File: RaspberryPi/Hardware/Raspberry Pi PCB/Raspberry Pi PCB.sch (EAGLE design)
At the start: 30 parts, among them Q11 BSS138, Q12 BSS138, Q2 BSS138, X1 0446200002

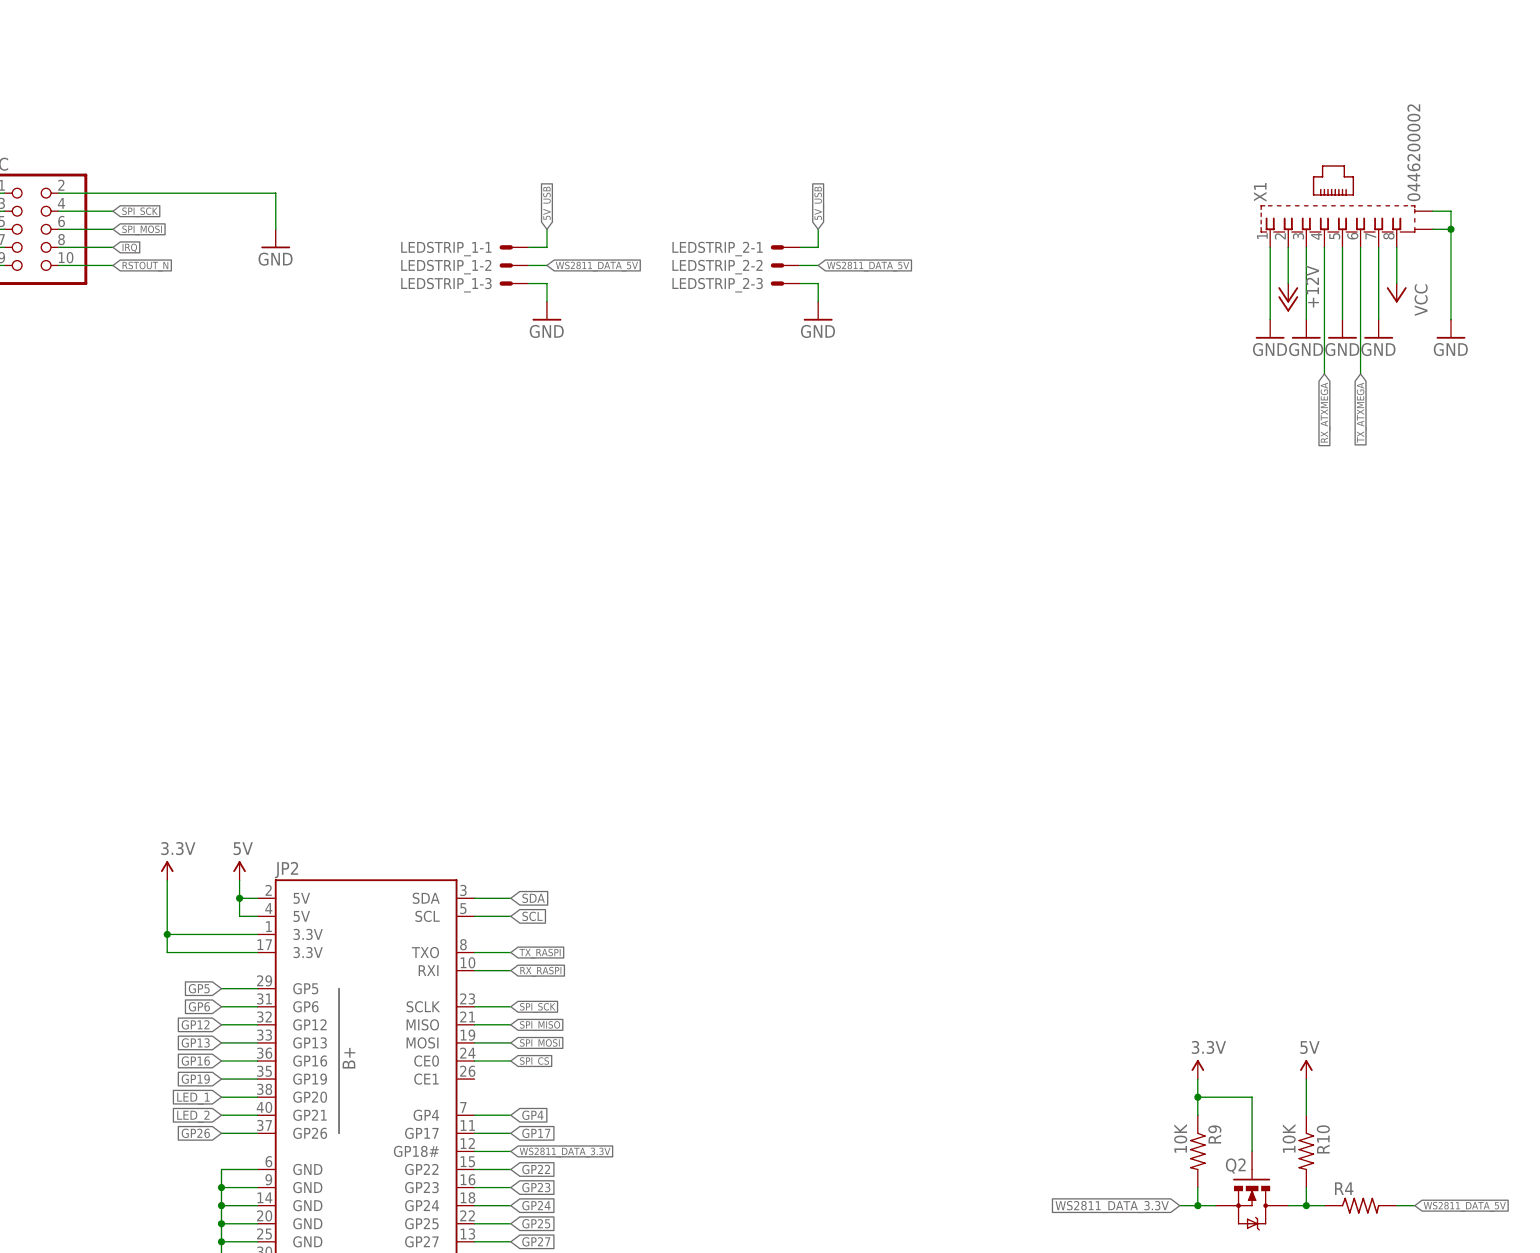
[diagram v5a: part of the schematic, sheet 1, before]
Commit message: Added a connector for the reed switch.
The reed switch is used to detect if the door is open. It works in combination with a magnet that is placed on the case itself.
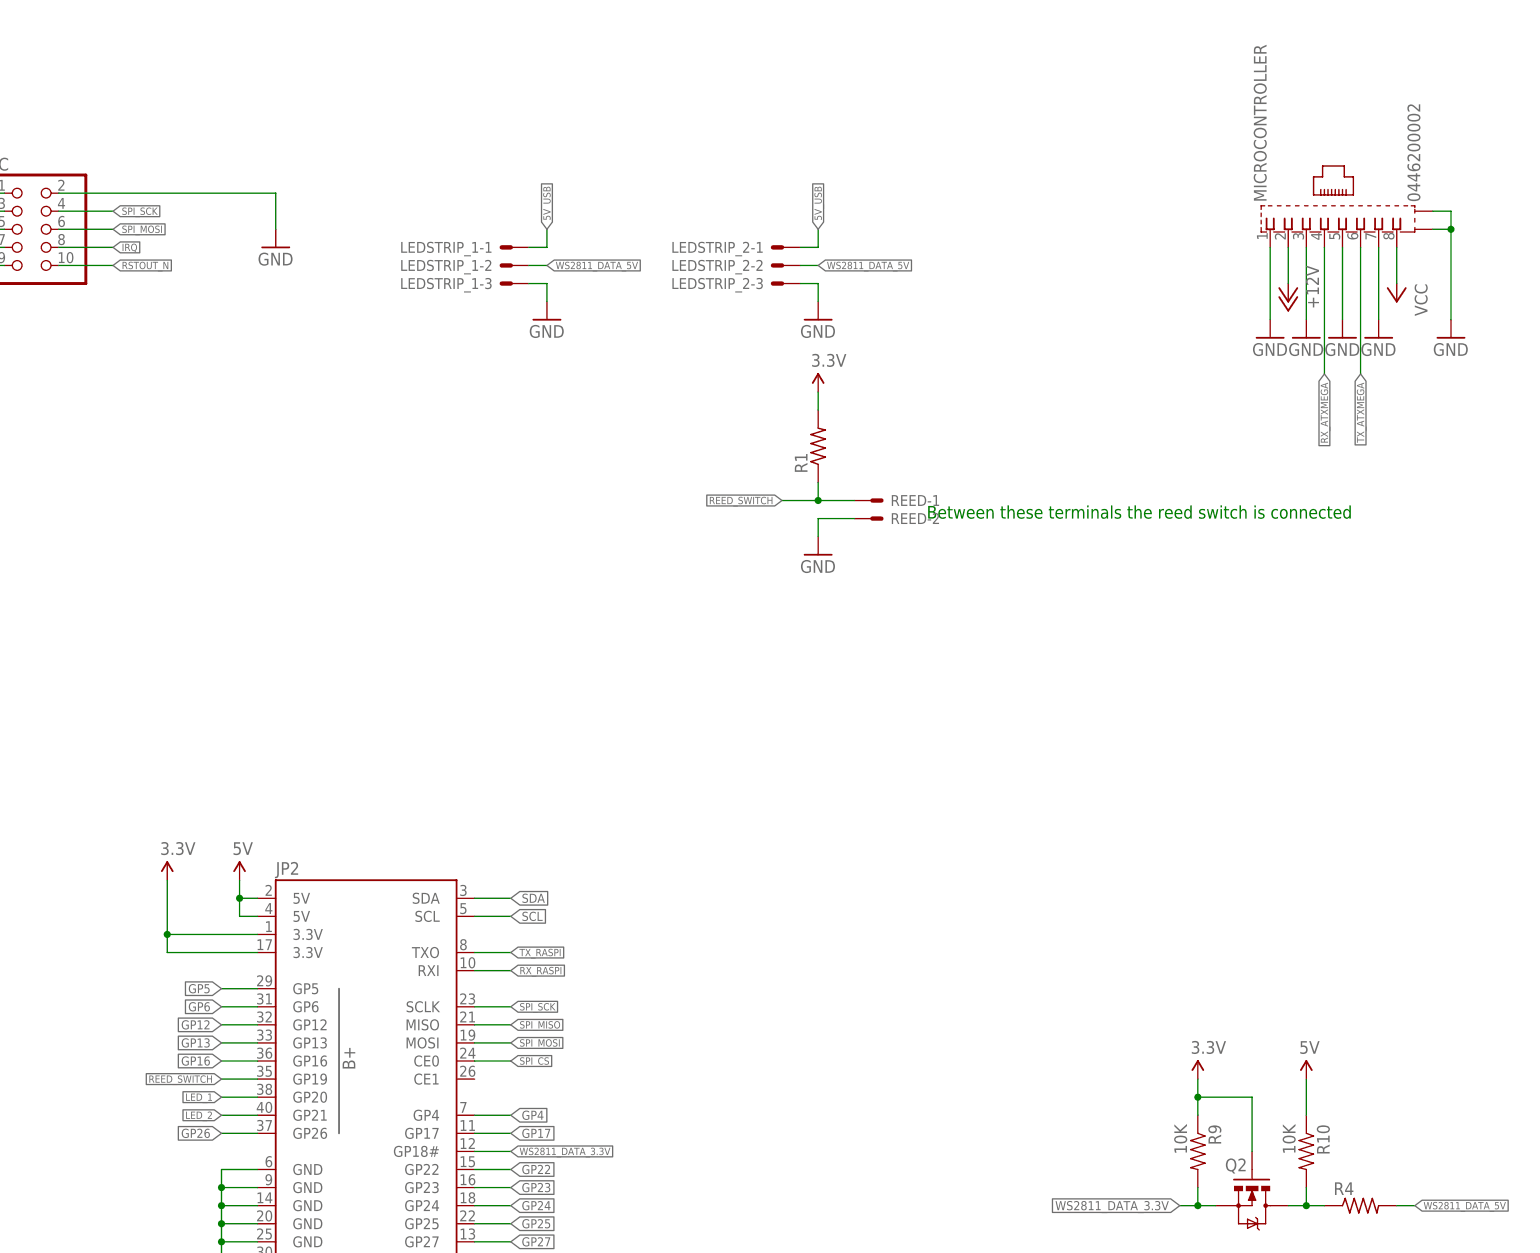
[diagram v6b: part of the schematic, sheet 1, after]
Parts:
- added R1: (no value), adafruit:R-US_R0805
- added REED: 22-05-7028-02, con-molex:22-05-7028-02
- renumbered USB1 to USB_POWER, X1 to MICROCONTROLLER
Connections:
- removed net GP19: JP2.GP19
- new net REED_SWITCH: JP2.GP19, R1.1, REED-1.S
- net 3.3V: now also R1.2
- net GND: now also REED-2.S
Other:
- note added: "Between these terminals the reed switch is connected"
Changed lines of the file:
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@@
 <part name="SUPPLY2" library="SparkFun-Aesthetics" deviceset="3.3V" device=""/>
 <part name="FRAME1" library="SparkFun-Aesthetics" library_urn="urn:adsk.eagle:library:507" deviceset="FRAME-A4L" device=""/>
-<part name="X1" library="con-molex" library_urn="urn:adsk.eagle:library:165" deviceset="0446200002" device=""/>
+<part name="MICROCONTROLLER" library="con-molex" library_urn="urn:adsk.eagle:library:165" deviceset="0446200002" device=""/>
 <part name="GND7" library="SparkFun" deviceset="GND" device=""/>
 <part name="GND8" library="SparkFun" deviceset="GND" device=""/>
@@
 <part name="C11" library="SparkFun-Capacitors" library_urn="urn:adsk.eagle:library:510" deviceset="1.0UF" device="-0805-25V-(+80/-20%)" package3d_urn="urn:adsk.eagle:package:37429/1" value="100nF"/>
 <part name="GND25" library="supply1" library_urn="urn:adsk.eagle:library:371" deviceset="GND" device=""/>
-<part name="USB1" library="87520-0010BLF" deviceset="87520-0010BLF" device=""/>
+<part name="USB_POWER" library="87520-0010BLF" deviceset="87520-0010BLF" device=""/>
 <part name="GND4" library="SparkFun" deviceset="GND" device=""/>
 <part name="C7" library="SparkFun-Capacitors" library_urn="urn:adsk.eagle:library:510" deviceset="1.0UF" device="-0805-25V-(+80/-20%)" package3d_urn="urn:adsk.eagle:package:37429/1" value="100nF"/>
+<part name="SUPPLY3" library="SparkFun-Aesthetics" deviceset="3.3V" device=""/>
+<part name="R1" library="adafruit" deviceset="R-US_" device="R0805"/>
+<part name="REED" library="con-molex" library_urn="urn:adsk.eagle:library:165" deviceset="22-?-02" device="05-7028"/>
+<part name="GND15" library="SparkFun" deviceset="GND" device=""/>
 </parts>
 <sheets>
 <sheet>
 <plain>
+<text x="182.88" y="121.92" size="1.778" layer="91">Between these terminals the reed switch is connected</text>
 </plain>
 <instances>
@@
 <instance part="SUPPLY2" gate="G$1" x="35.56" y="27.94"/>
 <instance part="FRAME1" gate="G$1" x="0" y="0"/>
-<instance part="X1" gate="P" x="241.3" y="162.56" rot="R90"/>
+<instance part="MICROCONTROLLER" gate="P" x="241.3" y="162.56" rot="R90"/>
 <instance part="GND7" gate="1" x="256.54" y="147.32"/>
 <instance part="GND8" gate="1" x="246.38" y="147.32"/>
@@
 <instance part="SUPPLY7" gate="G$1" x="220.98" y="43.18"/>
 <instance part="SUPPLY9" gate="G$1" x="236.22" y="43.18"/>
+<instance part="SUPPLY3" gate="G$1" x="167.64" y="139.7"/>
+<instance part="R1" gate="G$1" x="167.64" y="132.08" rot="R90"/>
+<instance part="REED" gate="-1" x="175.26" y="124.46" smashed="yes">
+<attribute name="NAME" x="177.8" y="123.698" size="1.524" layer="95"/>
+</instance>
+<instance part="REED" gate="-2" x="175.26" y="121.92"/>
+<instance part="GND15" gate="1" x="167.64" y="116.84"/>
 </instances>
 <busses>
@@
 </segment>
 <segment>
-<pinref part="X1" gate="P" pin="S2"/>
+<pinref part="MICROCONTROLLER" gate="P" pin="S2"/>
 <pinref part="GND7" gate="1" pin="GND"/>
 <wire x1="254" y1="165.1" x2="256.54" y2="165.1" width="0.1524" layer="91"/>
 <wire x1="256.54" y1="165.1" x2="256.54" y2="162.56" width="0.1524" layer="91"/>
-<pinref part="X1" gate="P" pin="S1"/>
+<pinref part="MICROCONTROLLER" gate="P" pin="S1"/>
 <wire x1="256.54" y1="162.56" x2="256.54" y2="149.86" width="0.1524" layer="91"/>
 <wire x1="254" y1="162.56" x2="256.54" y2="162.56" width="0.1524" layer="91"/>
@@
 <segment>
 <pinref part="GND13" gate="1" pin="GND"/>
-<pinref part="X1" gate="P" pin="1"/>
+<pinref part="MICROCONTROLLER" gate="P" pin="1"/>
 <wire x1="231.14" y1="149.86" x2="231.14" y2="160.02" width="0.1524" layer="91"/>
 </segment>
 <segment>
 <pinref part="GND12" gate="1" pin="GND"/>
-<pinref part="X1" gate="P" pin="3"/>
+<pinref part="MICROCONTROLLER" gate="P" pin="3"/>
 <wire x1="236.22" y1="149.86" x2="236.22" y2="160.02" width="0.1524" layer="91"/>
 </segment>
 <segment>
 <pinref part="GND11" gate="1" pin="GND"/>
-<pinref part="X1" gate="P" pin="5"/>
+<pinref part="MICROCONTROLLER" gate="P" pin="5"/>
 <wire x1="241.3" y1="149.86" x2="241.3" y2="160.02" width="0.1524" layer="91"/>
 </segment>
 <segment>
 <pinref part="GND8" gate="1" pin="GND"/>
-<pinref part="X1" gate="P" pin="7"/>
+<pinref part="MICROCONTROLLER" gate="P" pin="7"/>
 <wire x1="246.38" y1="149.86" x2="246.38" y2="160.02" width="0.1524" layer="91"/>
 </segment>
@@
 <pinref part="GND24" gate="1" pin="GND"/>
 <pinref part="LED2" gate="G$1" pin="C"/>
+</segment>
+<segment>
+<pinref part="REED" gate="-2" pin="S"/>
+<pinref part="GND15" gate="1" pin="GND"/>
+<wire x1="172.72" y1="121.92" x2="167.64" y2="121.92" width="0.1524" layer="91"/>
+<wire x1="167.64" y1="121.92" x2="167.64" y2="119.38" width="0.1524" layer="91"/>
 </segment>
 </net>
@@
 <pinref part="SUPPLY7" gate="G$1" pin="3.3V"/>
 </segment>
+<segment>
+<pinref part="R1" gate="G$1" pin="2"/>
+<pinref part="SUPPLY3" gate="G$1" pin="3.3V"/>
+<wire x1="167.64" y1="137.16" x2="167.64" y2="139.7" width="0.1524" layer="91"/>
+</segment>
 </net>
 <net name="GP4" class="0">
@@
 </segment>
 </net>
-<net name="GP19" class="0">
+<net name="REED_SWITCH" class="0">
 <segment>
 <pinref part="JP2" gate="G$1" pin="GP19"/>
 <wire x1="88.9" y1="43.18" x2="83.82" y2="43.18" width="0.1524" layer="91"/>
-<label x="83.82" y="43.18" size="1.27" layer="95" rot="R180" xref="yes"/>
+<label x="83.82" y="43.18" size="1.016" layer="95" rot="R180" xref="yes"/>
+</segment>
+<segment>
+<pinref part="R1" gate="G$1" pin="1"/>
+<pinref part="REED" gate="-1" pin="S"/>
+<wire x1="167.64" y1="127" x2="167.64" y2="124.46" width="0.1524" layer="91"/>
+<wire x1="167.64" y1="124.46" x2="172.72" y2="124.46" width="0.1524" layer="91"/>
+<wire x1="167.64" y1="124.46" x2="162.56" y2="124.46" width="0.1524" layer="91"/>
+<junction x="167.64" y="124.46"/>
+<label x="162.56" y="124.46" size="1.016" layer="95" rot="R180" xref="yes"/>
 </segment>
 </net>
@@
 <pinref part="JP2" gate="G$1" pin="GP20"/>
 <wire x1="88.9" y1="40.64" x2="83.82" y2="40.64" width="0.1524" layer="91"/>
-<label x="83.82" y="40.64" size="1.27" layer="95" rot="R180" xref="yes"/>
+<label x="83.82" y="40.64" size="1.016" layer="95" rot="R180" xref="yes"/>
 </segment>
 <segment>
@@
 <pinref part="JP2" gate="G$1" pin="GP21"/>
 <wire x1="88.9" y1="38.1" x2="83.82" y2="38.1" width="0.1524" layer="91"/>
-<label x="83.82" y="38.1" size="1.27" layer="95" rot="R180" xref="yes"/>
+<label x="83.82" y="38.1" size="1.016" layer="95" rot="R180" xref="yes"/>
 </segment>
 <segment>
@@
 <segment>
 <pinref part="P+1" gate="1" pin="+12V"/>
-<pinref part="X1" gate="P" pin="2"/>
+<pinref part="MICROCONTROLLER" gate="P" pin="2"/>
 <wire x1="233.68" y1="154.94" x2="233.68" y2="160.02" width="0.1524" layer="91"/>
 </segment>
@@
 </segment>
 <segment>
-<pinref part="X1" gate="P" pin="4"/>
+<pinref part="MICROCONTROLLER" gate="P" pin="4"/>
 <wire x1="238.76" y1="160.02" x2="238.76" y2="142.24" width="0.1524" layer="91"/>
 <label x="238.76" y="142.24" size="1.016" layer="95" rot="R270" xref="yes"/>
@@
 </segment>
 <segment>
-<pinref part="X1" gate="P" pin="6"/>
+<pinref part="MICROCONTROLLER" gate="P" pin="6"/>
 <wire x1="243.84" y1="160.02" x2="243.84" y2="142.24" width="0.1524" layer="91"/>
 <label x="243.84" y="142.24" size="1.016" layer="95" rot="R270" xref="yes"/>
@@
 <segment>
 <pinref part="P+5" gate="VCC" pin="VCC"/>
-<pinref part="X1" gate="P" pin="8"/>
+<pinref part="MICROCONTROLLER" gate="P" pin="8"/>
 <wire x1="248.92" y1="154.94" x2="248.92" y2="160.02" width="0.1524" layer="91"/>
 </segment>
@@
 <instance part="C11" gate="G$1" x="-10.16" y="124.46"/>
 <instance part="GND25" gate="1" x="-10.16" y="116.84"/>
-<instance part="USB1" gate="G$1" x="172.72" y="124.46"/>
+<instance part="USB_POWER" gate="G$1" x="172.72" y="124.46"/>
 <instance part="GND4" gate="1" x="157.48" y="114.3"/>
 <instance part="C7" gate="G$1" x="157.48" y="121.92"/>
@@
 </segment>
 <segment>
-<pinref part="USB1" gate="G$1" pin="GND"/>
+<pinref part="USB_POWER" gate="G$1" pin="GND"/>
 <pinref part="C7" gate="G$1" pin="2"/>
 <wire x1="167.64" y1="119.38" x2="157.48" y2="119.38" width="0.1524" layer="91"/>
@@
 </segment>
 <segment>
-<pinref part="USB1" gate="G$1" pin="VCC"/>
+<pinref part="USB_POWER" gate="G$1" pin="VCC"/>
 <wire x1="157.48" y1="129.54" x2="157.48" y2="127" width="0.1524" layer="91"/>
 <wire x1="157.48" y1="127" x2="167.64" y2="127" width="0.1524" layer="91"/>
